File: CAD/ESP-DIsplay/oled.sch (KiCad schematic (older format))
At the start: 1 part, among them J601 OLED

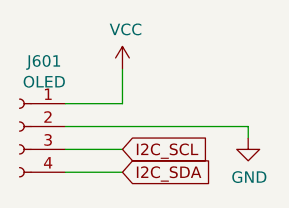
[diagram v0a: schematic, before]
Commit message: esp12e adc pinsadded, 1117 power module
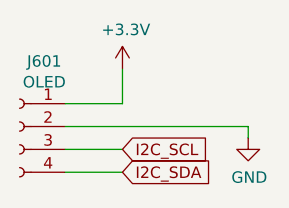
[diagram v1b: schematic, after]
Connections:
- net VCC renamed +3V3
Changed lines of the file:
@@
-	1    0    0    -1
-$EndComp
-$Comp
-L power:VCC #PWR?
-U 1 1 60C872C5
-P 5400 3200
-AR Path="/60C872C5" Ref="#PWR?"  Part="1"
-AR Path="/60C58A4D/60C5A6B7/60C872C5" Ref="#PWR0601"  Part="1"
-F 0 "#PWR0601" H 5400 3050 50  0001 C CNN
-F 1 "VCC" H 5415 3373 50  0000 C CNN
-F 2 "" H 5400 3200 50  0001 C CNN
-F 3 "" H 5400 3200 50  0001 C CNN
-	1    5400 3200
 	1    0    0    -1
 $EndComp
@@
 	-1   0    0    -1
 $EndComp
+$Comp
+L power:+3.3V #PWR0111
+U 1 1 603CDEA6
+P 5400 3200
+F 0 "#PWR0111" H 5400 3050 50  0001 C CNN
+F 1 "+3.3V" H 5415 3373 50  0000 C CNN
+F 2 "" H 5400 3200 50  0001 C CNN
+F 3 "" H 5400 3200 50  0001 C CNN
+	1    5400 3200
+	1    0    0    -1
+$EndComp
 $EndSCHEMATC
